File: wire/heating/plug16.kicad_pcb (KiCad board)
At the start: 2 copper layers, 64 x 64 mm, 15 parts, among them J1 Moat_Bus_16, J10 1wireConn, J2 Moat_Bus_wire, J3 SCLK, J4 SDA, J5 3V3, J6 GND, J8 S1, J9 S2, Q1 2N7002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

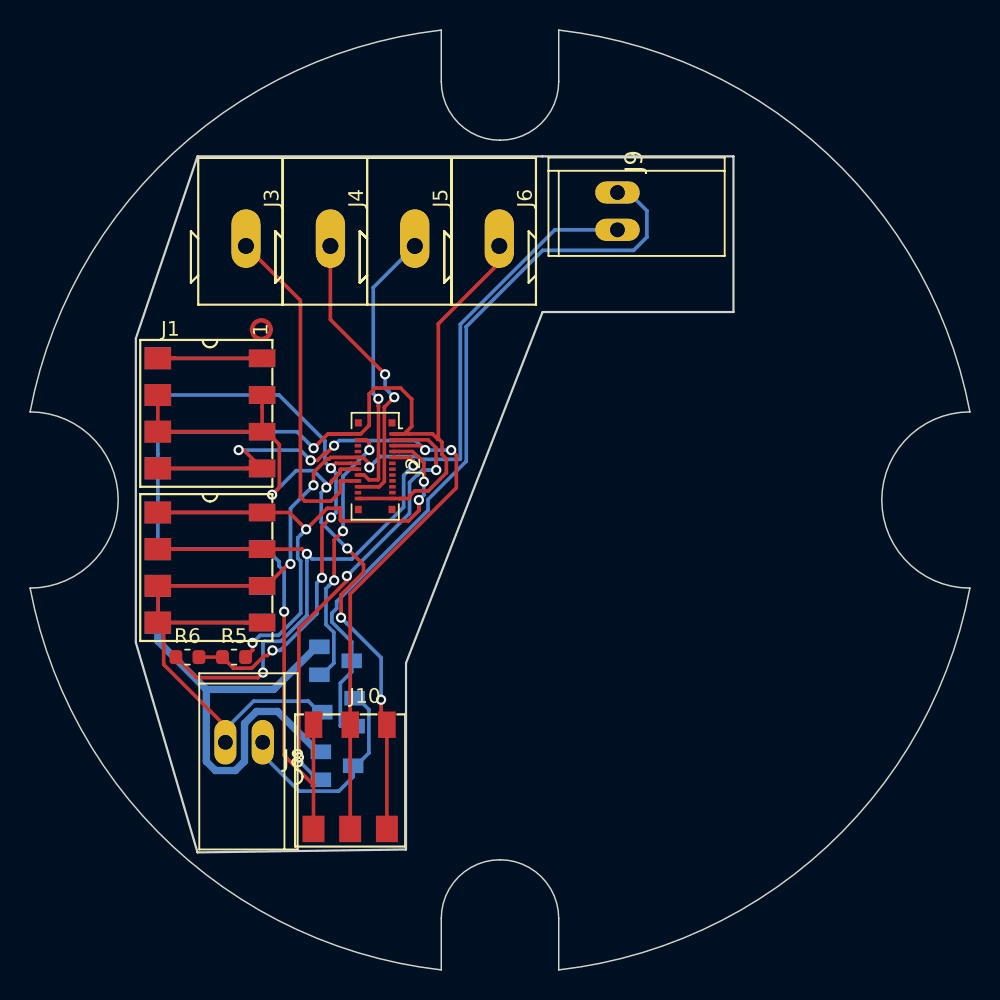
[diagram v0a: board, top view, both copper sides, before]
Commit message: Heating: fix connector, add OSHW, etc.
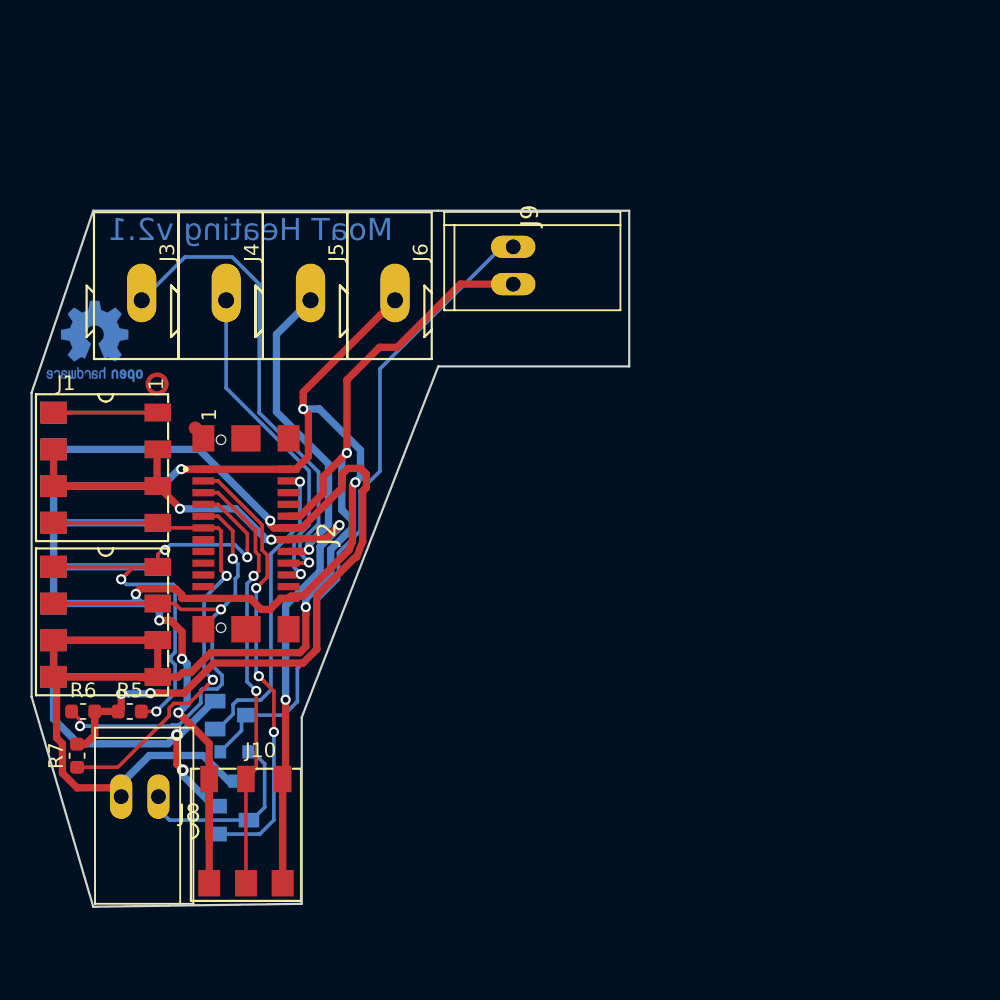
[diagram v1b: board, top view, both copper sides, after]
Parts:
- removed U$1: Val**, localstuff:UNTERPUTZDOSE
- added R7: 470, Resistor_SMD:R_0603_1608Metric, F.Cu at (22.4, 66.6)
- added REF**: OSHW-Logo2_7.3x6mm_Copper, Symbol:OSHW-Logo2_7.3x6mm_Copper, B.Cu at (23.6, 38.4)
- D1: value BAS40-05 -> BAT54C; footprint localstuff:SOT23 -> Package_TO_SOT_SMD:SOT-23
- J2: footprint localstuff:Molex_SlimStack_503772-24 -> localstuff:TE_1775014_socket
- moved J2 9.93 mm to (33.9, 51.5)
- moved J10 8.01 mm to (33.9, 71.8)
- moved J4 8.01 mm to (32.5, 35.6)
- moved J5 8.01 mm to (38.3, 35.6)
- moved J6 8.01 mm to (44.0, 35.6)
- moved J8 8.01 mm to (26.7, 69.4)
- moved Q1 8.01 mm to (33.0, 71.0)
- moved Q2 8.01 mm to (32.9, 63.9)
- moved R6 8.01 mm to (22.8, 63.6)
- moved D1 8.01 mm to (33.1, 67.3)
- moved J1 8.01 mm to (24.4, 52.3)
- moved J3 8.01 mm to (26.8, 35.6)
- moved J9 8.01 mm to (52.1, 33.2)
- moved R5 8.01 mm to (26.0, 63.6)
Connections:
- J10 pad 2: Net-(J1-Pad7) -> Net-(J10-Pad2)
- J2 pad 11: (no net) -> Net-(J1-Pad7)
- J2 pad 13: (no net) -> Net-(J2-Pad13)
- J2 pad 15: (no net) -> Net-(J2-Pad15)
- J2 pad 17: (no net) -> Net-(J2-Pad17)
- J2 pad 19: (no net) -> Net-(J2-Pad19)
- J2 pad 21: (no net) -> Net-(J2-Pad21)
- J2 pad 22: (no net) -> Net-(J2-Pad22)
- J2 pad 5: Net-(J1-Pad7) -> Net-(J10-Pad2)
- J2 pad 6: (no net) -> Net-(J2-Pad6)
- J2 pad 8: (no net) -> Net-(J2-Pad8)
- J8 pad 1: Net-(D1-Pad1) -> Net-(D1-Pad2)
- J9 pad 1: Net-(D1-Pad2) -> Net-(D1-Pad1)
- Q1 pad 3: Net-(D1-Pad1) -> Net-(D1-Pad2)
- Q2 pad 3: Net-(D1-Pad2) -> Net-(D1-Pad1)
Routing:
- net Net-(D1-Pad2): track 52.0 -> 13.1 mm
- net Net-(J10-Pad2): track 0.00 -> 29.6 mm, vias 0 -> 2
- net Net-(D1-Pad1): track 14.9 -> 44.5 mm
- net Net-(J1-Pad4): track 37.1 -> 59.8 mm, vias 4 -> 3
- net Net-(J1-Pad7): track 57.2 -> 36.0 mm, vias 5 -> 2
- net Net-(D1-Pad3): track 79.7 -> 93.0 mm, vias 3 -> 2
- net GNDPWR: track 48.8 -> 38.6 mm, vias 0 -> 2
- net Net-(J2-Pad18): track 23.7 -> 32.8 mm, vias 0 -> 1
- net Net-(J1-Pad10): track 107.6 -> 116.3 mm, vias 2 -> 7
- net Net-(J2-Pad16): track 18.8 -> 21.4 mm
- net /S2: track 18.6 -> 21.1 mm, vias 3 -> 1
- net Net-(J2-Pad20): track 20.1 -> 22.5 mm, vias 2 -> 1
- net Net-(J1-Pad11): track 40.0 -> 38.2 mm
- net Net-(J1-Pad3): track 52.8 -> 53.6 mm, vias 5 -> 4
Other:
- board size 64 x 64 mm -> 40.7 x 47.4 mm
- board text added: "MoaT Heating v2.1"

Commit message: ?
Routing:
- net Net-(J1-Pad10): track 116.3 -> 113.5 mm
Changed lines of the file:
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@@
     (thickness 1.6)
     (drawings 23)
-    (tracks 392)
+    (tracks 393)
     (zones 0)
     (modules 16)
@@
   )
   (setup
-    (last_trace_width 0.5)
+    (last_trace_width 0.25)
     (user_trace_width 0.25)
     (user_trace_width 0.5)
@@
   (via (at 26.4 55.6) (size 0.7) (drill 0.4) (layers F.Cu B.Cu) (net 6))
   (segment (start 26.75 56.25) (end 26.4 55.9) (width 0.5) (layer B.Cu) (net 6))
-  (segment (start 38.149999 43.349999) (end 37.8 43) (width 0.5) (layer F.Cu) (net 6))
-  (segment (start 36.8 47.1) (end 37.3 47.1) (width 0.5) (layer F.Cu) (net 6))
-  (segment (start 38.149999 46.250001) (end 38.149999 43.349999) (width 0.5) (layer F.Cu) (net 6))
-  (segment (start 37.3 47.1) (end 38.149999 46.250001) (width 0.5) (layer F.Cu) (net 6))
-  (via (at 37.8 43) (size 0.7) (drill 0.4) (layers F.Cu B.Cu) (net 6))
-  (segment (start 37.8 42.2) (end 37.8 43) (width 0.5) (layer F.Cu) (net 6))
-  (segment (start 44.05 35.6) (end 37.8 41.85) (width 0.5) (layer F.Cu) (net 6))
-  (segment (start 37.8 41.85) (end 37.8 42.2) (width 0.5) (layer F.Cu) (net 6))
   (segment (start 26.599999 55.400001) (end 26.4 55.6) (width 0.5) (layer F.Cu) (net 6))
   (segment (start 26.599999 55.329999) (end 26.599999 55.400001) (width 0.5) (layer F.Cu) (net 6))
@@
   (via (at 41.35001 48) (size 0.7) (drill 0.4) (layers F.Cu B.Cu) (net 6))
   (segment (start 41.150002 52.031513) (end 41.150002 48.200008) (width 0.5) (layer F.Cu) (net 6))
-  (segment (start 37.8 43) (end 38.894974 43) (width 0.5) (layer B.Cu) (net 6))
   (segment (start 36.8 55.9) (end 36.949999 55.750001) (width 0.5) (layer F.Cu) (net 6))
   (segment (start 37.77612 55.750001) (end 40.93049 52.595631) (width 0.5) (layer F.Cu) (net 6))
   (segment (start 41.150002 48.200008) (end 41.35001 48) (width 0.5) (layer F.Cu) (net 6))
-  (segment (start 38.894974 43) (end 41.700009 45.805035) (width 0.5) (layer B.Cu) (net 6))
   (segment (start 36.949999 55.750001) (end 37.77612 55.750001) (width 0.5) (layer F.Cu) (net 6))
-  (segment (start 41.700009 47.650001) (end 41.35001 48) (width 0.5) (layer B.Cu) (net 6))
-  (segment (start 41.700009 45.805035) (end 41.700009 47.650001) (width 0.5) (layer B.Cu) (net 6))
+  (via (at 39.7 45.2) (size 0.7) (drill 0.4) (layers F.Cu B.Cu) (net 6))
+  (segment (start 44.05 35.6) (end 39.7 39.95) (width 0.5) (layer F.Cu) (net 6))
+  (segment (start 41.700009 47.650001) (end 41.700009 45.805035) (width 0.5) (layer B.Cu) (net 6))
+  (segment (start 39.7 39.95) (end 39.7 44.705026) (width 0.5) (layer F.Cu) (net 6))
+  (segment (start 41.35001 48) (end 41.700009 47.650001) (width 0.5) (layer B.Cu) (net 6))
+  (segment (start 41.094974 45.2) (end 40.194974 45.2) (width 0.5) (layer B.Cu) (net 6))
+  (segment (start 40.194974 45.2) (end 39.7 45.2) (width 0.5) (layer B.Cu) (net 6))
+  (segment (start 39.7 44.705026) (end 39.7 45.2) (width 0.5) (layer F.Cu) (net 6))
+  (segment (start 37.3 47.1) (end 39.2 45.2) (width 0.5) (layer F.Cu) (net 6))
+  (segment (start 41.700009 45.805035) (end 41.094974 45.2) (width 0.5) (layer B.Cu) (net 6))
+  (segment (start 39.205026 45.2) (end 39.7 45.2) (width 0.5) (layer F.Cu) (net 6))
+  (segment (start 39.2 45.2) (end 39.205026 45.2) (width 0.5) (layer F.Cu) (net 6))
+  (segment (start 36.8 47.1) (end 37.3 47.1) (width 0.5) (layer F.Cu) (net 6))
   (segment (start 20.8 56.25) (end 27.9 56.25) (width 0.25) (layer F.Cu) (net 7))
   (segment (start 32 50.3) (end 33 51.3) (width 0.25) (layer F.Cu) (net 7))
